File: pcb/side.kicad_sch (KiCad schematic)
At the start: 46 parts, among them J1 R0, J10 R3, J2 C0, J3 R3, J4 C2, J5 Conn_01x12_Socket, J6 Conn_01x12_Socket, J7 C0, J8 R0, J9 C2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

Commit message: small updates
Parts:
- added H1, H2, H3, H4: MountingHole, zzkeeb:Hole_M2, symbol Mechanical:MountingHole

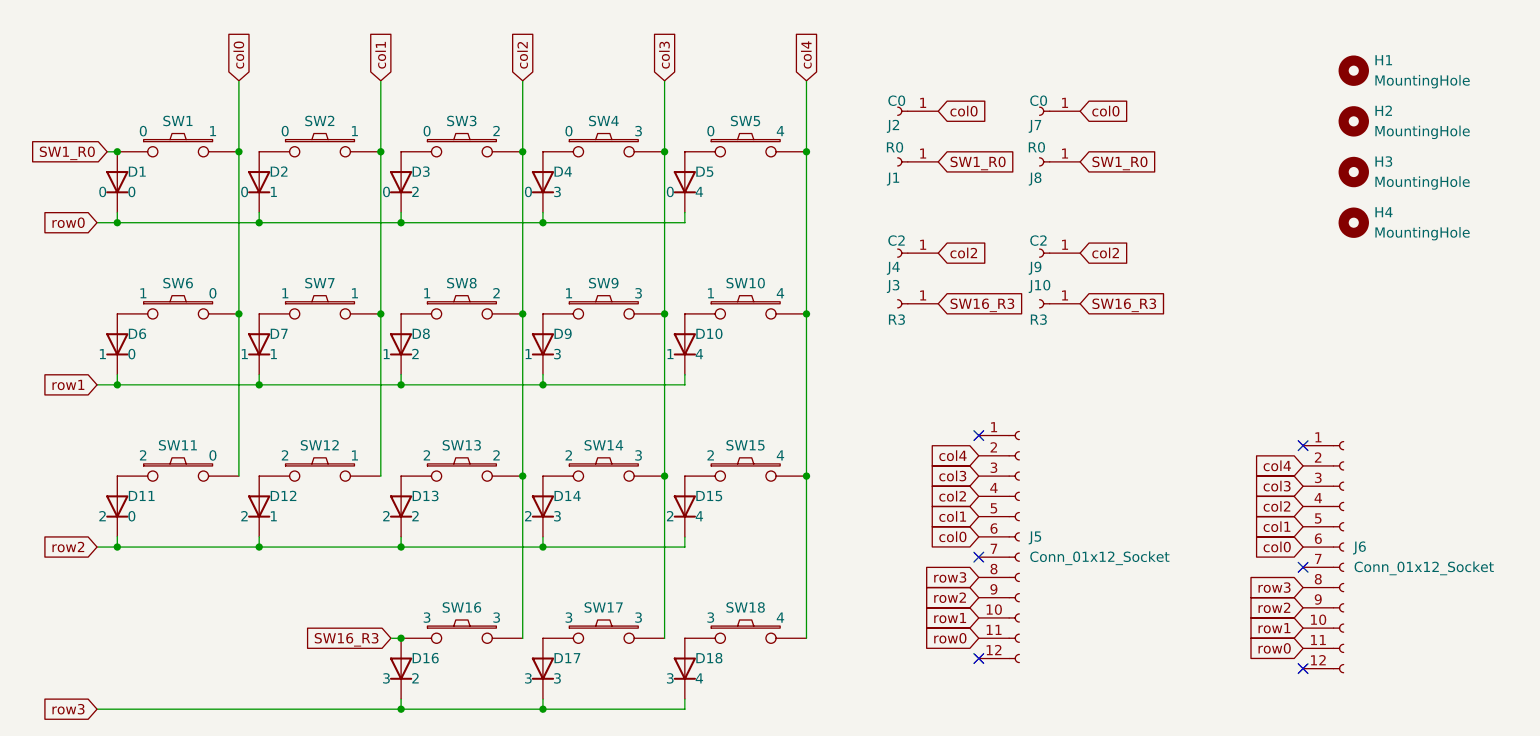
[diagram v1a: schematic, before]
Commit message: jumpers for VIK GPIO, small side updates
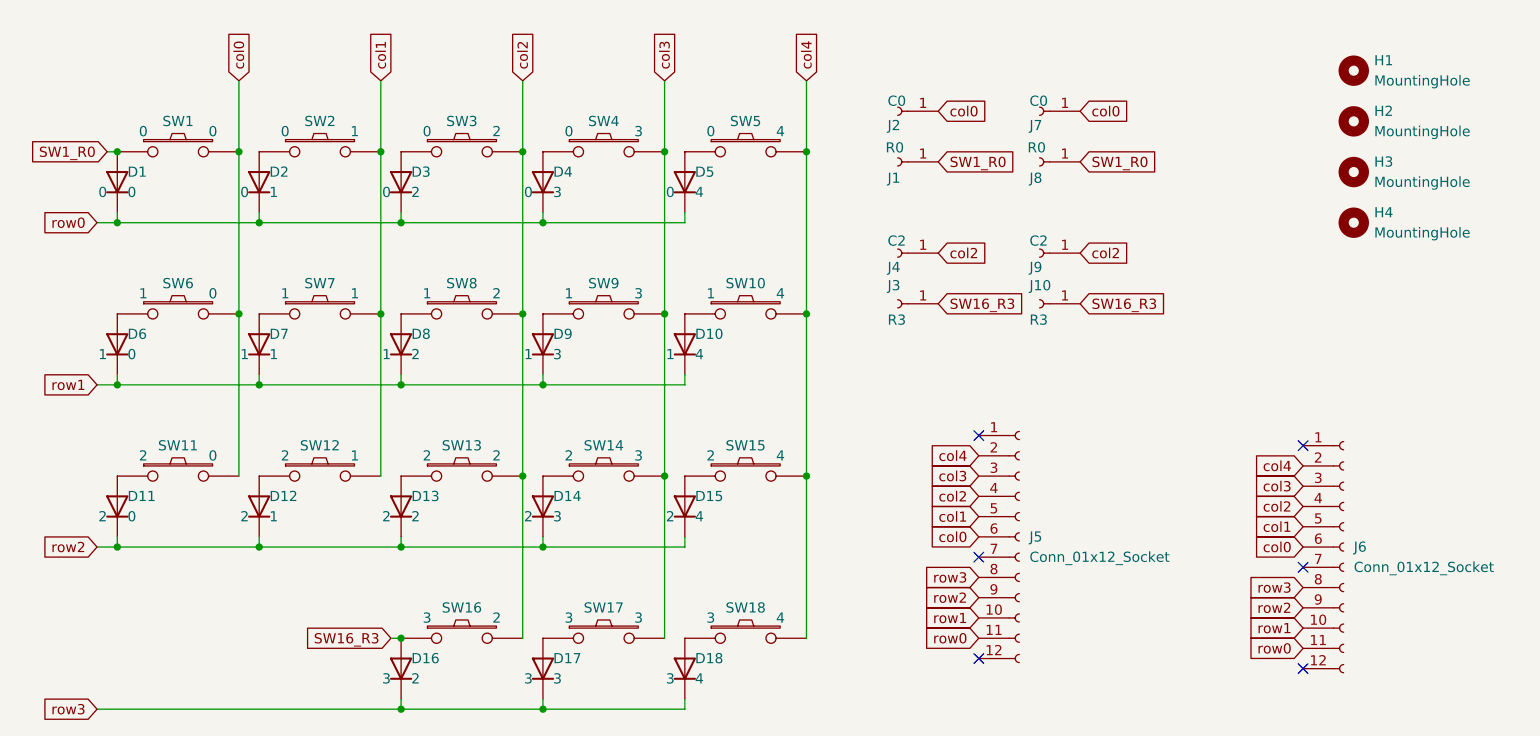
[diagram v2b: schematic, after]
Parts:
- J1, J10, J2, J3, J4, J7, J8, J9: footprint TestPoint:TestPoint_Pad_D1.5mm -> TestPoint:TestPoint_THTPad_D1.5mm_Drill0.7mm
- SW1: col 1 -> 0
- SW16: col 3 -> 2
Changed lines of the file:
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@@
 			)
 		)
-		(property "col" "1"
+		(property "col" "0"
 			(at 69.85 68.58 0)
 			(do_not_autoplace yes)
@@
 			)
 		)
-		(property "Footprint" "TestPoint:TestPoint_Pad_D1.5mm"
+		(property "Footprint" "TestPoint:TestPoint_THTPad_D1.5mm_Drill0.7mm"
 			(at 173.99 90.17 0)
 			(effects
@@
 			)
 		)
-		(property "Footprint" "TestPoint:TestPoint_Pad_D1.5mm"
+		(property "Footprint" "TestPoint:TestPoint_THTPad_D1.5mm_Drill0.7mm"
 			(at 156.21 90.17 0)
 			(effects
@@
 			)
 		)
-		(property "Footprint" "TestPoint:TestPoint_Pad_D1.5mm"
+		(property "Footprint" "TestPoint:TestPoint_THTPad_D1.5mm_Drill0.7mm"
 			(at 156.21 72.39 0)
 			(effects
@@
 			)
 		)
-		(property "Footprint" "TestPoint:TestPoint_Pad_D1.5mm"
+		(property "Footprint" "TestPoint:TestPoint_THTPad_D1.5mm_Drill0.7mm"
 			(at 156.21 66.04 0)
 			(effects
@@
 			)
 		)
-		(property "col" "3"
+		(property "col" "2"
 			(at 105.41 129.54 0)
 			(do_not_autoplace yes)
@@
 			)
 		)
-		(property "Footprint" "TestPoint:TestPoint_Pad_D1.5mm"
+		(property "Footprint" "TestPoint:TestPoint_THTPad_D1.5mm_Drill0.7mm"
 			(at 173.99 72.39 0)
 			(effects
@@
 			)
 		)
-		(property "Footprint" "TestPoint:TestPoint_Pad_D1.5mm"
+		(property "Footprint" "TestPoint:TestPoint_THTPad_D1.5mm_Drill0.7mm"
 			(at 173.99 83.82 0)
 			(effects
@@
 			)
 		)
-		(property "Footprint" "TestPoint:TestPoint_Pad_D1.5mm"
+		(property "Footprint" "TestPoint:TestPoint_THTPad_D1.5mm_Drill0.7mm"
 			(at 173.99 66.04 0)
 			(effects
@@
 			)
 		)
-		(property "Footprint" "TestPoint:TestPoint_Pad_D1.5mm"
+		(property "Footprint" "TestPoint:TestPoint_THTPad_D1.5mm_Drill0.7mm"
 			(at 156.21 83.82 0)
 			(effects
